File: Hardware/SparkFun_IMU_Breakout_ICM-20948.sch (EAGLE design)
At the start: 60 parts, among them Q1 DMN2005LP4K-7, Q10 RE1C002UN, Q11 DMN2005LP4K-7, Q12 RE1C002UN, Q13 DMN2005LP4K-7, Q14 RE1C002UN, Q15 DMN2005LP4K-7, Q16 RE1C002UN, Q2 RE1C002UN, Q3 DMN2005LP4K-7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

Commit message: Laid out v30
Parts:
- removed Q1, Q11, Q13, Q15, Q3, Q5, Q7, Q9: DMN2005LP4K-7, new_fets:DMN2005LP4K-7
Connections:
- net AUX_CL_VIN_JMP renamed N$4
- net AUX_DA_VIN_JMP renamed N$5
- net SCL/SCLK_VIN_JMP renamed N$2
- net SDA/SDI_VIN_JMP renamed N$3
- net !CS: no longer Q1.S
- net !CS!_VIN: no longer Q1.D
- net 1.8V: no longer Q1.G, Q11.G, Q13.G, Q15.G, Q3.G, Q5.G, Q7.G, Q9.G
- net AD0/SDO: no longer Q3.S
- net AD0/SDO_VIN: no longer Q3.D
- net AUX_CL: no longer Q11.S
- net AUX_CL_VIN: now also J4.5; no longer J4.3, Q11.D
- net AUX_DA: no longer Q9.S
- net AUX_DA_VIN: now also J4.4; no longer J4.2, Q9.D
- net FSYNC: no longer Q13.S
- net FSYNC_VIN: now also J4.3; no longer J4.4, Q13.D
- net INT: no longer Q15.S
- net INT_VIN: now also J4.2; no longer J4.5, Q15.D
- net SCL/SCLK: no longer Q5.S
- net SCL/SCLK_VIN: no longer Q5.D
- net SDA/SDI: no longer Q7.S
- net SDA/SDI_VIN: no longer Q7.D
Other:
- note added: "Address Option"
- note added: "I2C Level Shifting + Pullup Disconnects"
- note added: "SPI / Interrupt Level Shifting"
- note removed: "Level Shifting"
- note removed: "Options"
- moved on the sheet: C4, D1, JP2, JP3, JP4, JP5, Q10, Q12, Q14, Q16, Q2, Q4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

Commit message: Ran board design checklist ahead of the review
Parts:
- FRAME2: REV v21 -> v30
- Q10, Q12, Q14, Q16, Q2, Q4, Q6, Q8: value RE1C002UN -> 20V/0.2A/8MHz/1.2Ω/1Vth; device new_fets:RE1C002UN -> SparkFun-DiscreteSemi:MOSFET-NCH-RE1C002UN
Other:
- moved on the sheet: JP2, JP4, R14, R15, R16, R17

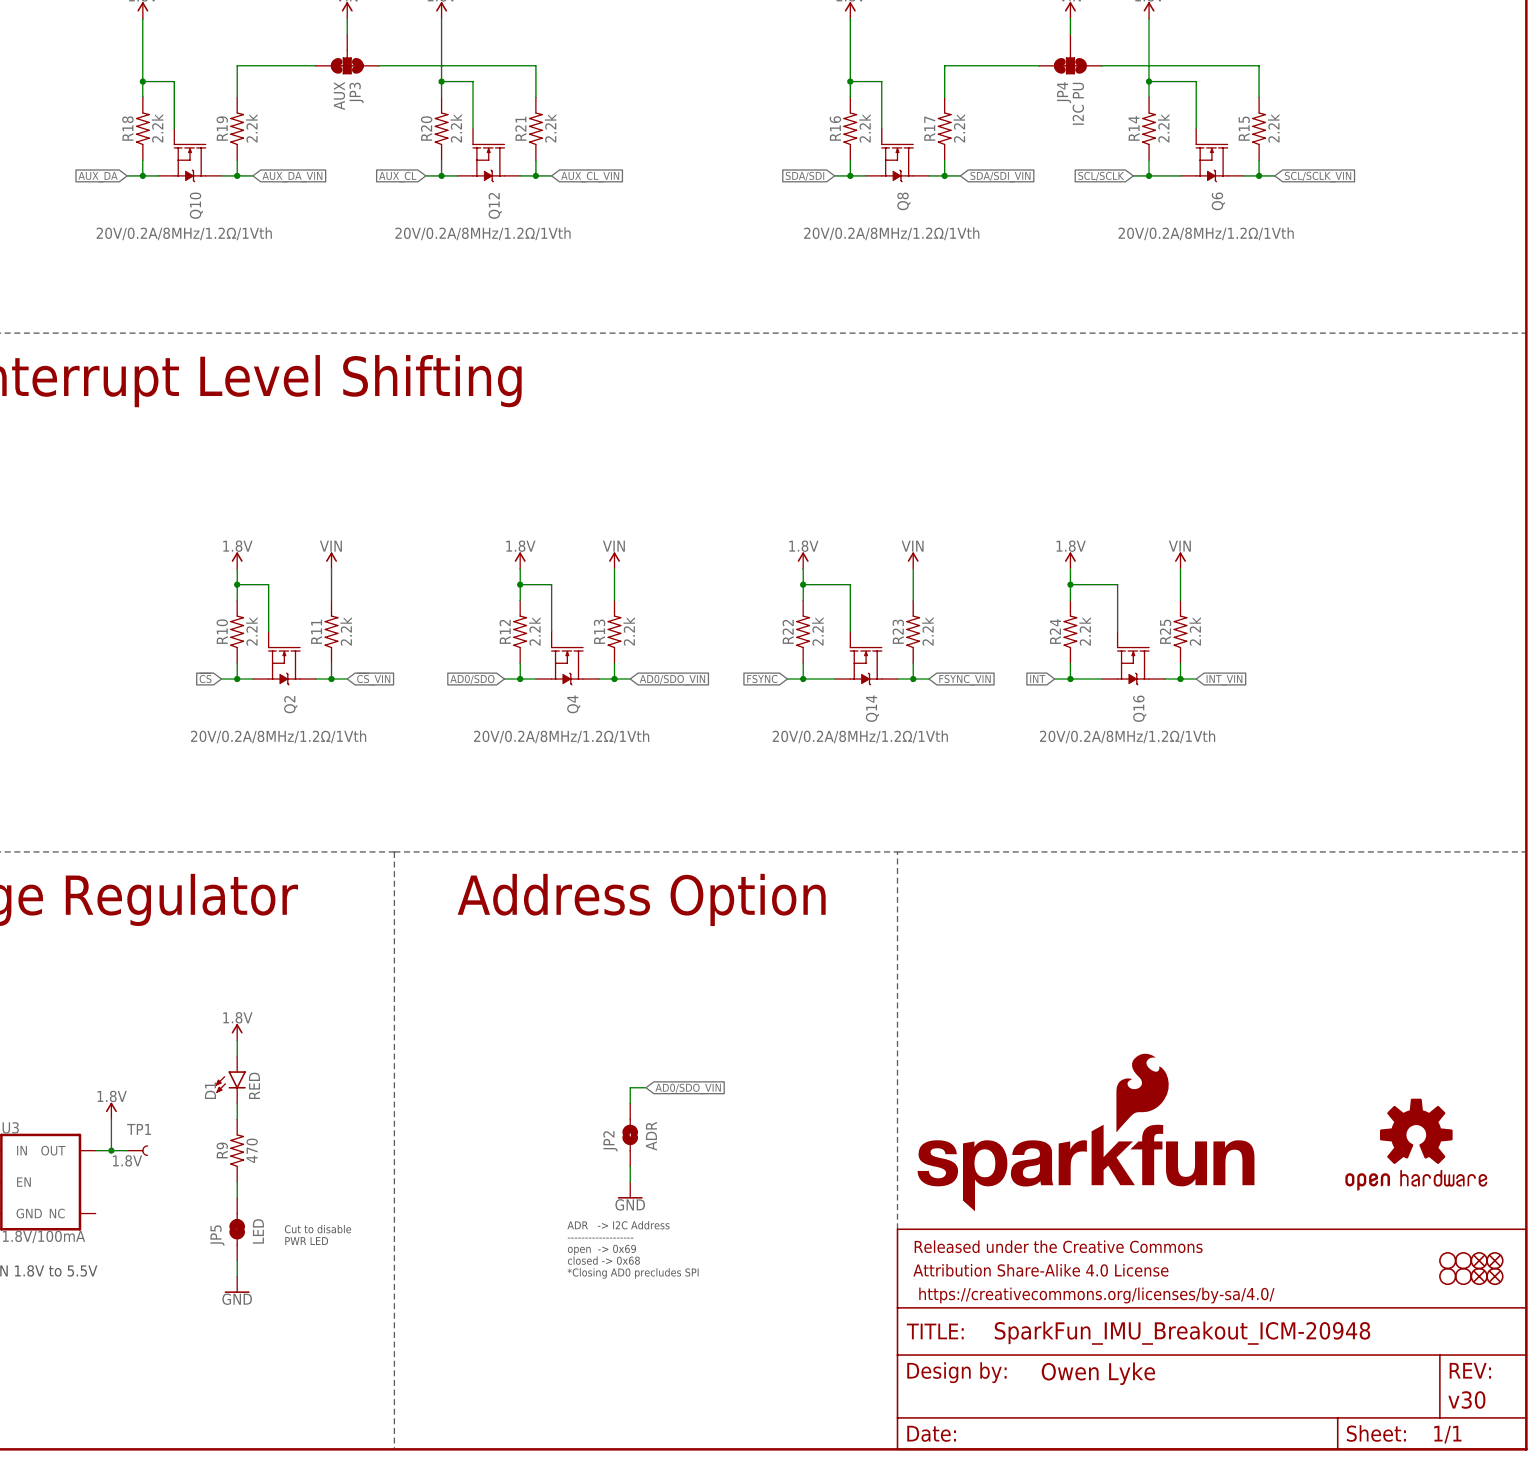
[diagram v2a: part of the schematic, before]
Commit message: Changes from design review
Level shifter circuit spacing
Axes indicators
Routing touch-ups
LED resistor change
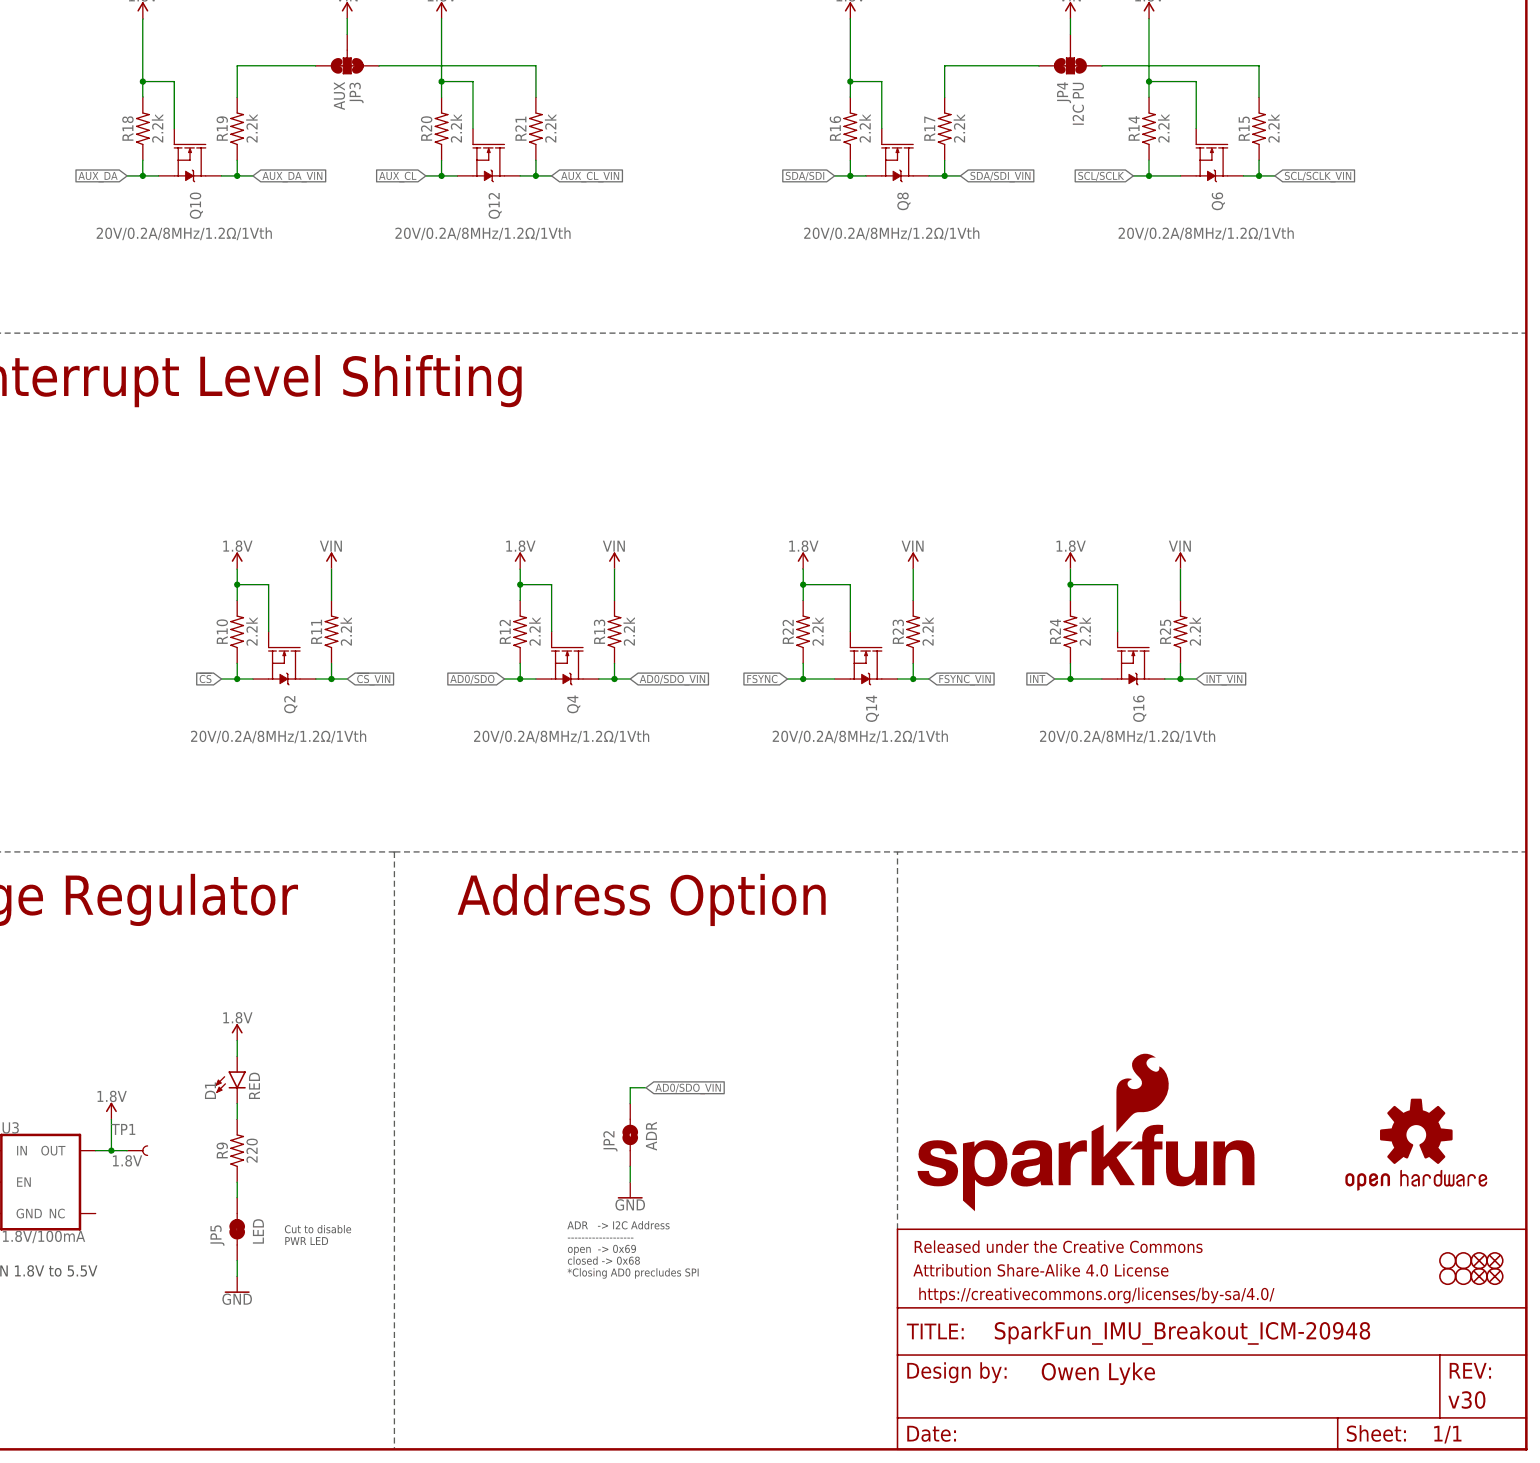
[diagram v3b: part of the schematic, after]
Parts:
- R9: value 470 -> 220; device SparkFun-Resistors:470OHM-0603-1/10W-1% -> SparkFun-Resistors:220OHM-0603-1/10W-1%
